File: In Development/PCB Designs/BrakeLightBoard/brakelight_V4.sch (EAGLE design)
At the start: 17 parts, among them Q1 30N06L, Q2 30N06L

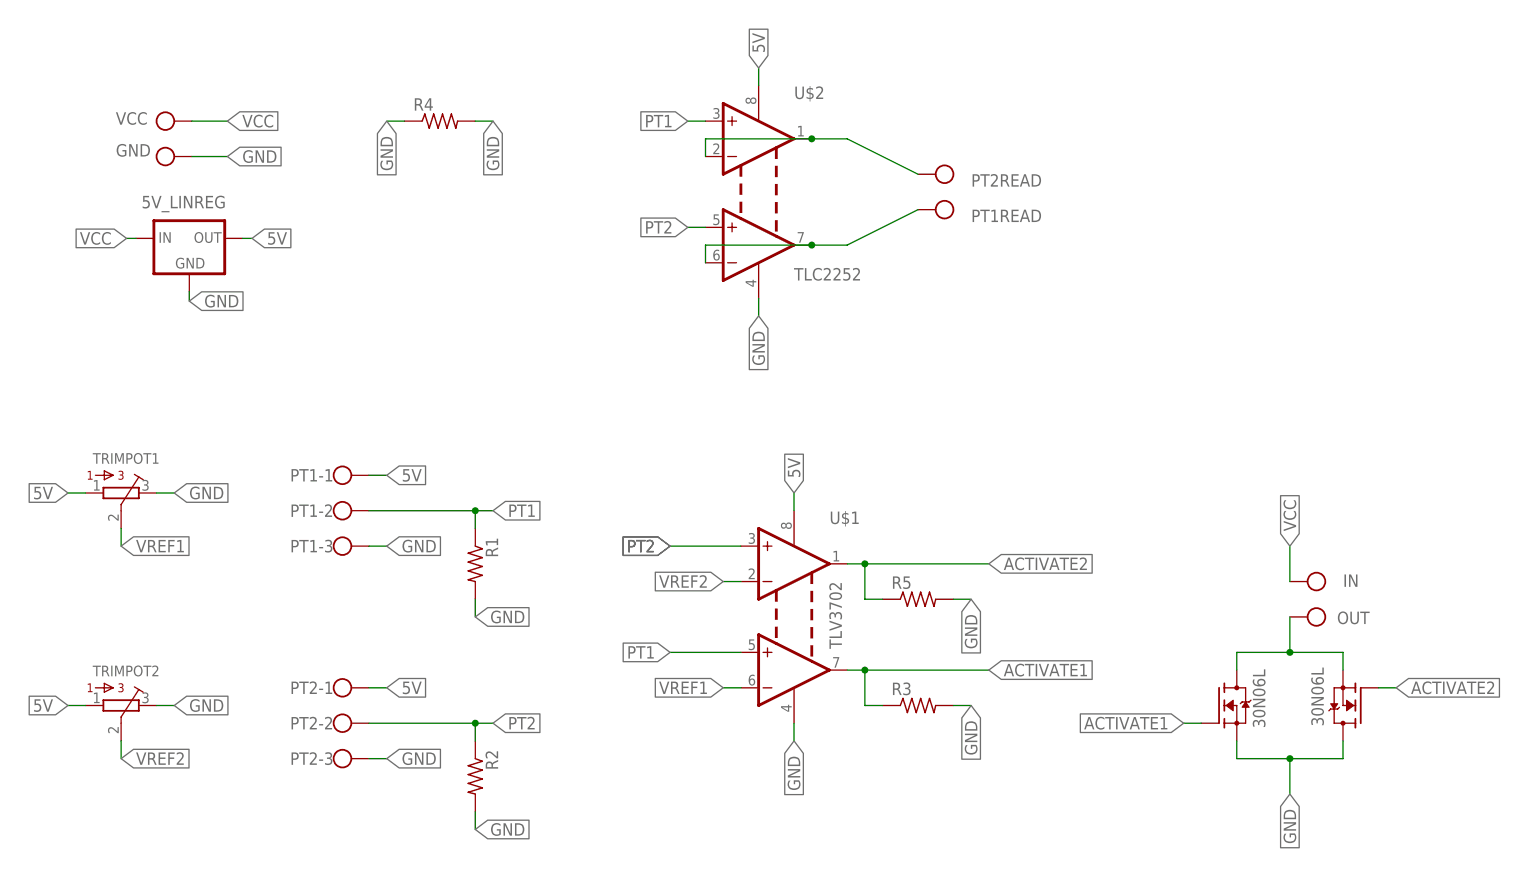
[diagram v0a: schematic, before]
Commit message: Created brd for brakelight_V4
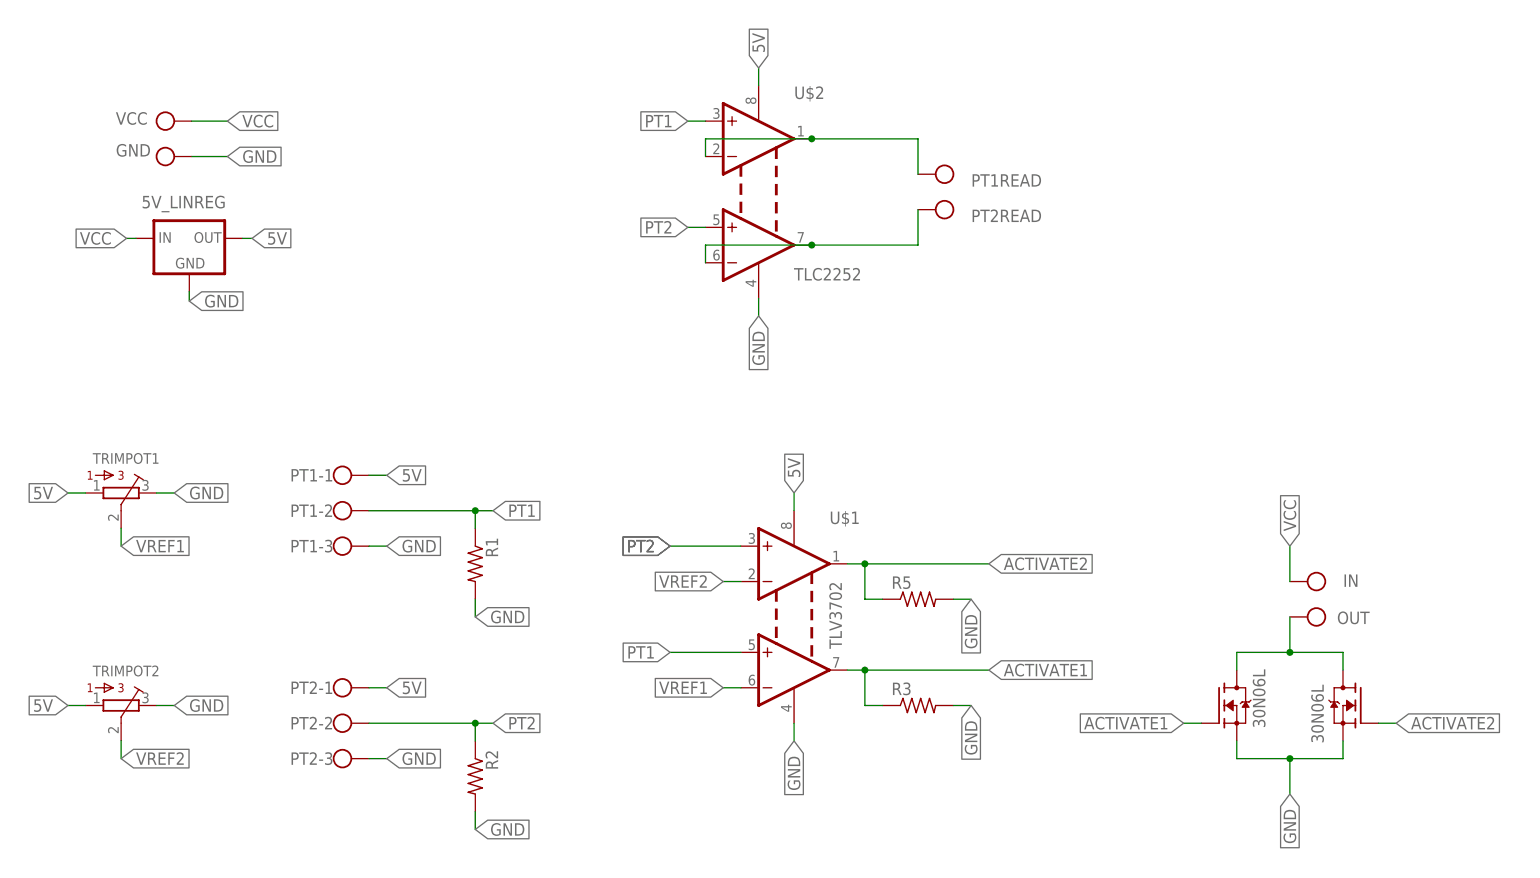
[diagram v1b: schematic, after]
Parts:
- removed R4: (no value), 0ohmresistor:R-US_0207/5V
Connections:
- net GND: now also Q1.S; no longer Q1.D, R4.1, R4.2
- net N$2: now also Q1.D; no longer Q1.S
- net N$6: now also INO_READ-1.KL; no longer INO_READ-2.KL
- net N$7: now also INO_READ-2.KL; no longer INO_READ-1.KL
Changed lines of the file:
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@@
 <part name="TRIMPOT2" library="bourns" deviceset="3386-" device="Y"/>
 <part name="R3" library="0ohmresistor" deviceset="R-US_" device="0207/5V" package3d_urn="urn:adsk.eagle:package:23502/1"/>
-<part name="R4" library="0ohmresistor" deviceset="R-US_" device="0207/5V" package3d_urn="urn:adsk.eagle:package:23502/1"/>
 <part name="U$2" library="GTOR" deviceset="TLC2252" device=""/>
 <part name="Q1" library="FQP30N06L" deviceset="FQP30N06L" device="" value="30N06L">
@@
 <attribute name="GND" x="-82.042" y="66.04" size="1.778" layer="96" display="name"/>
 </instance>
-<instance part="INO_READ" gate="-1" x="38.1" y="58.42" smashed="yes" rot="R180">
-<attribute name="PT1READ" x="50.8" y="58.42" size="1.778" layer="96" rot="R180" display="name"/>
-</instance>
-<instance part="INO_READ" gate="-2" x="38.1" y="63.5" smashed="yes" rot="R180">
-<attribute name="VALUE" x="40.64" y="67.183" size="1.778" layer="96" rot="R180"/>
-<attribute name="PT2READ" x="50.8" y="63.5" size="1.778" layer="96" rot="R180" display="name"/>
+<instance part="INO_READ" gate="-1" x="38.1" y="63.5" smashed="yes" rot="R180">
+<attribute name="PT1READ" x="50.8" y="63.5" size="1.778" layer="96" rot="R180" display="name"/>
+</instance>
+<instance part="INO_READ" gate="-2" x="38.1" y="58.42" smashed="yes" rot="R180">
+<attribute name="VALUE" x="40.64" y="62.103" size="1.778" layer="96" rot="R180"/>
+<attribute name="PT2READ" x="50.8" y="58.42" size="1.778" layer="96" rot="R180" display="name"/>
 </instance>
 <instance part="R1" gate="G$1" x="-30.48" y="7.62" smashed="yes" rot="R270">
@@
 <attribute name="VALUE" x="29.21" y="-16.002" size="1.778" layer="96"/>
 </instance>
-<instance part="R4" gate="G$1" x="-35.56" y="71.12" smashed="yes">
-<attribute name="NAME" x="-39.37" y="72.6186" size="1.778" layer="95"/>
-<attribute name="VALUE" x="-39.37" y="67.818" size="1.778" layer="96"/>
-</instance>
 <instance part="U$2" gate="G$1" x="10.16" y="53.34" smashed="yes">
 <attribute name="VALUE" x="15.24" y="48.26" size="1.778" layer="96"/>
 <attribute name="NAME" x="15.24" y="74.295" size="1.778" layer="95"/>
 </instance>
-<instance part="Q1" gate="G$1" x="96.52" y="-12.7" smashed="yes" rot="R180">
-<attribute name="VALUE" x="91.219" y="-15.699" size="1.778" layer="96" rot="R90"/>
+<instance part="Q1" gate="G$1" x="96.52" y="-12.7" smashed="yes" rot="MR0">
+<attribute name="VALUE" x="91.219" y="-9.701" size="1.778" layer="96" rot="MR270"/>
 </instance>
 <instance part="R5" gate="G$1" x="33.02" y="2.54" smashed="yes">
@@
 </segment>
 <segment>
-<pinref part="R4" gate="G$1" pin="1"/>
-<wire x1="-40.64" y1="71.12" x2="-43.18" y2="71.12" width="0.1524" layer="91"/>
-<label x="-43.18" y="71.12" size="1.778" layer="95" rot="R270" xref="yes"/>
-</segment>
-<segment>
-<pinref part="R4" gate="G$1" pin="2"/>
-<wire x1="-30.48" y1="71.12" x2="-27.94" y2="71.12" width="0.1524" layer="91"/>
-<label x="-27.94" y="71.12" size="1.778" layer="95" rot="R270" xref="yes"/>
-</segment>
-<segment>
 <pinref part="U$2" gate="G$1" pin="V-"/>
 <wire x1="10.16" y1="45.72" x2="10.16" y2="43.18" width="0.1524" layer="91"/>
@@
 </segment>
 <segment>
-<pinref part="Q1" gate="G$1" pin="D"/>
-<wire x1="93.98" y1="-17.78" x2="93.98" y2="-20.32" width="0.1524" layer="91"/>
 <pinref part="Q2" gate="G$1" pin="S"/>
 <wire x1="93.98" y1="-20.32" x2="86.36" y2="-20.32" width="0.1524" layer="91"/>
@@
 <junction x="86.36" y="-20.32"/>
 <label x="86.36" y="-25.4" size="1.778" layer="95" rot="R270" xref="yes"/>
+<pinref part="Q1" gate="G$1" pin="S"/>
+<wire x1="93.98" y1="-17.78" x2="93.98" y2="-20.32" width="0.1524" layer="91"/>
 </segment>
 </net>
@@
 <wire x1="17.78" y1="68.58" x2="2.54" y2="68.58" width="0.1524" layer="91"/>
 <wire x1="2.54" y1="68.58" x2="2.54" y2="66.04" width="0.1524" layer="91"/>
-<pinref part="INO_READ" gate="-2" pin="KL"/>
-<wire x1="17.78" y1="68.58" x2="22.86" y2="68.58" width="0.1524" layer="91"/>
-<wire x1="22.86" y1="68.58" x2="33.02" y2="63.5" width="0.1524" layer="91"/>
+<pinref part="INO_READ" gate="-1" pin="KL"/>
+<wire x1="17.78" y1="68.58" x2="33.02" y2="68.58" width="0.1524" layer="91"/>
+<wire x1="33.02" y1="68.58" x2="33.02" y2="63.5" width="0.1524" layer="91"/>
 <junction x="17.78" y="68.58"/>
 </segment>
@@
 <wire x1="17.78" y1="53.34" x2="2.54" y2="53.34" width="0.1524" layer="91"/>
 <wire x1="2.54" y1="53.34" x2="2.54" y2="50.8" width="0.1524" layer="91"/>
-<pinref part="INO_READ" gate="-1" pin="KL"/>
-<wire x1="17.78" y1="53.34" x2="22.86" y2="53.34" width="0.1524" layer="91"/>
-<wire x1="22.86" y1="53.34" x2="33.02" y2="58.42" width="0.1524" layer="91"/>
+<pinref part="INO_READ" gate="-2" pin="KL"/>
+<wire x1="33.02" y1="58.42" x2="33.02" y2="53.34" width="0.1524" layer="91"/>
+<wire x1="33.02" y1="53.34" x2="17.78" y2="53.34" width="0.1524" layer="91"/>
 <junction x="17.78" y="53.34"/>
 </segment>
@@
 <wire x1="86.36" y1="-5.08" x2="93.98" y2="-5.08" width="0.1524" layer="91"/>
 <junction x="86.36" y="-5.08"/>
-<pinref part="Q1" gate="G$1" pin="S"/>
+<pinref part="Q1" gate="G$1" pin="D"/>
 <wire x1="93.98" y1="-5.08" x2="93.98" y2="-7.62" width="0.1524" layer="91"/>
 </segment>
@@
 <net name="ACTIVATE2" class="0">
 <segment>
-<pinref part="Q1" gate="G$1" pin="G"/>
-<wire x1="99.06" y1="-10.16" x2="101.6" y2="-10.16" width="0.1524" layer="91"/>
-<label x="101.6" y="-10.16" size="1.778" layer="95" xref="yes"/>
-</segment>
-<segment>
 <wire x1="25.4" y1="2.54" x2="27.94" y2="2.54" width="0.1524" layer="91"/>
 <pinref part="R5" gate="G$1" pin="1"/>
@@
 <label x="43.18" y="7.62" size="1.778" layer="95" xref="yes"/>
 </segment>
-</net>
+<segment>
+<pinref part="Q1" gate="G$1" pin="G"/>
+<wire x1="99.06" y1="-15.24" x2="101.6" y2="-15.24" width="0.1524" layer="91"/>
+<label x="101.6" y="-15.24" size="1.778" layer="95" xref="yes"/>
+</segment>
+</net>

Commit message: small revisions
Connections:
- removed net N$1: R3.2
- removed net N$3: R5.2
- net GND: now also R3.2, R5.2
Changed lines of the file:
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@@
-</segment>
-<segment>
-<label x="40.64" y="-12.7" size="1.778" layer="95" rot="R270" xref="yes"/>
 </segment>
 <segment>
@@
 <wire x1="10.16" y1="45.72" x2="10.16" y2="43.18" width="0.1524" layer="91"/>
 <label x="10.16" y="43.18" size="1.778" layer="95" rot="R270" xref="yes"/>
-</segment>
-<segment>
-<label x="40.64" y="2.54" size="1.778" layer="95" rot="R270" xref="yes"/>
 </segment>
 <segment>
@@
 <pinref part="Q1" gate="G$1" pin="S"/>
 <wire x1="93.98" y1="-17.78" x2="93.98" y2="-20.32" width="0.1524" layer="91"/>
+</segment>
+<segment>
+<wire x1="38.1" y1="2.54" x2="40.64" y2="2.54" width="0.1524" layer="91"/>
+<pinref part="R5" gate="G$1" pin="2"/>
+<label x="40.64" y="2.54" size="1.778" layer="95" xref="yes"/>
+</segment>
+<segment>
+<wire x1="38.1" y1="-12.7" x2="40.64" y2="-12.7" width="0.1524" layer="91"/>
+<pinref part="R3" gate="G$1" pin="2"/>
+<label x="40.64" y="-12.7" size="1.778" layer="95" xref="yes"/>
 </segment>
 </net>
@@
 </segment>
 </net>
-<net name="N$1" class="0">
-<segment>
-<wire x1="38.1" y1="-12.7" x2="40.64" y2="-12.7" width="0.1524" layer="91"/>
-<pinref part="R3" gate="G$1" pin="2"/>
-</segment>
-</net>
 <net name="N$6" class="0">
 <segment>
@@
 <wire x1="33.02" y1="53.34" x2="17.78" y2="53.34" width="0.1524" layer="91"/>
 <junction x="17.78" y="53.34"/>
-</segment>
-</net>
-<net name="N$3" class="0">
-<segment>
-<wire x1="38.1" y1="2.54" x2="40.64" y2="2.54" width="0.1524" layer="91"/>
-<pinref part="R5" gate="G$1" pin="2"/>
 </segment>
 </net>
@@
 </sheet>
 </sheets>
-<errors>
-</errors>
 </schematic>
 </drawing>
